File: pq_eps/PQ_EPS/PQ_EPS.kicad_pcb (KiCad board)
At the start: 4 copper layers, 40 x 40 mm, 80 parts, among them IC1 DS2782E+, IC2 ISL9120IRTNZ, J1 SLW-110-01-T-S, J2 SLW-110-01-T-S, J4 SLW-110-01-T-S, Q1 SIR424DP-T1-GE3, U1 SPV1040TTR, U2 SPV1040TTR, U3 SPV1040TTR, U4 LTC4040EUFD#PBF

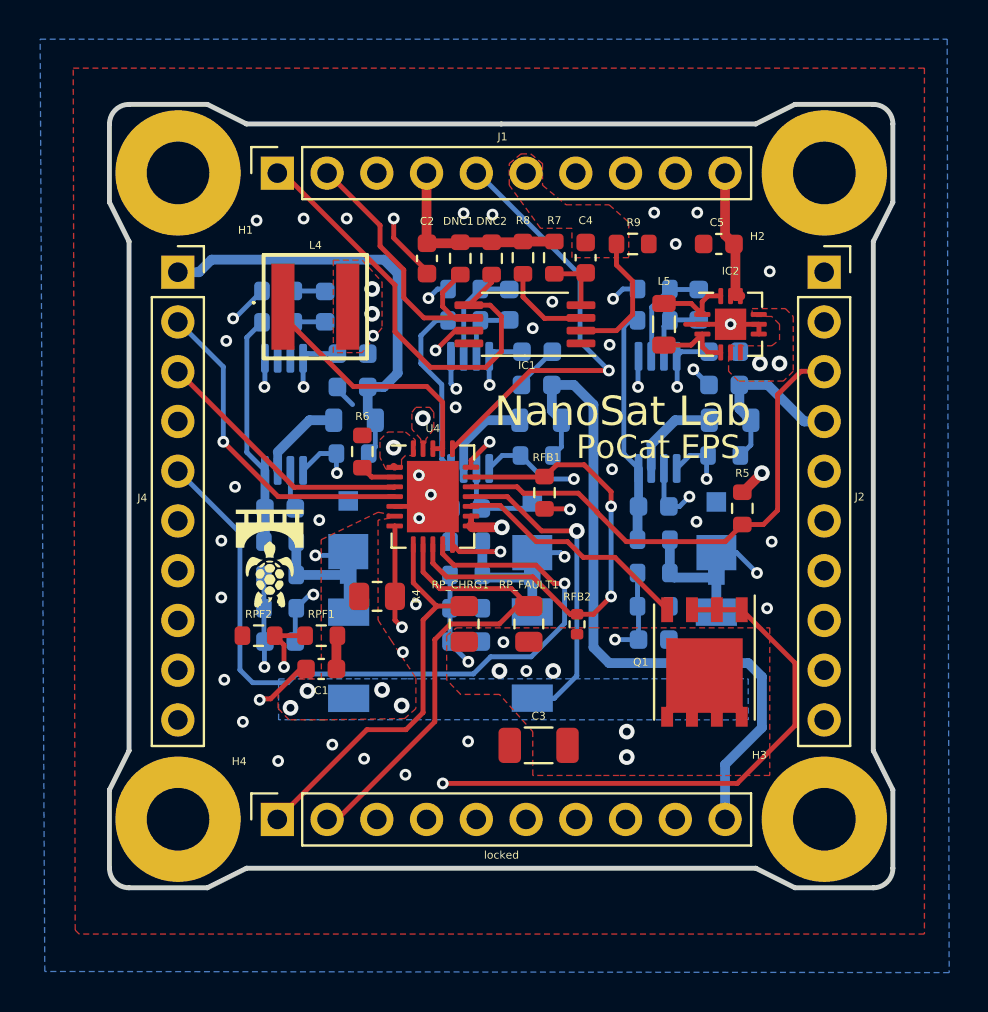
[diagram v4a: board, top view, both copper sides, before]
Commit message: Full Kicad7 transition, library improvement and adaptation, correct footprints and 3D models added
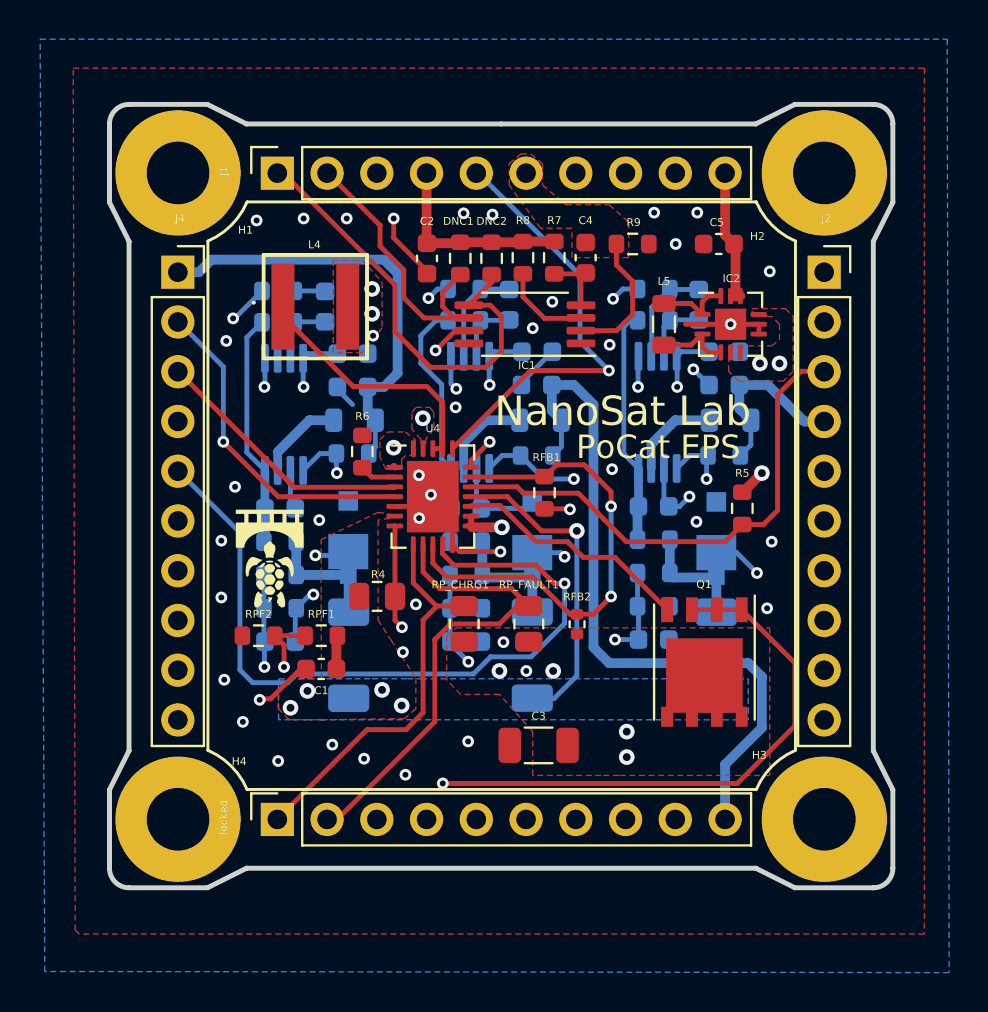
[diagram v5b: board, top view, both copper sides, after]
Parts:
- Annotation1: footprint symbols-nsl:Bridgemaker -> -nsl_symbols:Bridgemaker
- Annotation2: footprint symbols-nsl:NakNak -> -nsl_symbols:NakNak
- D1, D2, D3: footprint passive-nsl:SMM4F15ATR -> -nsl_passive:SMM4F15ATR
- D4, D5, D6: footprint Diode_SMD:D_SOD-128 -> -nsl_passive:RBS1LAM40ATR_Schottky
- IC2: footprint Package_DFN_QFN:QFN-12-1EP_3x3mm_P0.5mm_EP1.6x1.6mm -> -nsl_power:ISL9120IRTNZ
- J1, J2, J4, locked: footprint connector-nsl:SLW-110-01 -> -nsl_connector:SLW-110-01
- L4: footprint passive-nsl:XAL5030222MEC -> -nsl_passive:XAL5030222MEC
- Q1: value SIR424DP-T1-GE3 -> ~; footprint Package_SO:PowerPAK_SO-8_Single -> -nsl_power:SIR424DP

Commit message: Added adaptive resistive network for battery chemistry and charge voltage flexibility & connected all the PoLs + COMMS to 3V3_perm instead of VCC (3.3V - schottky diode)
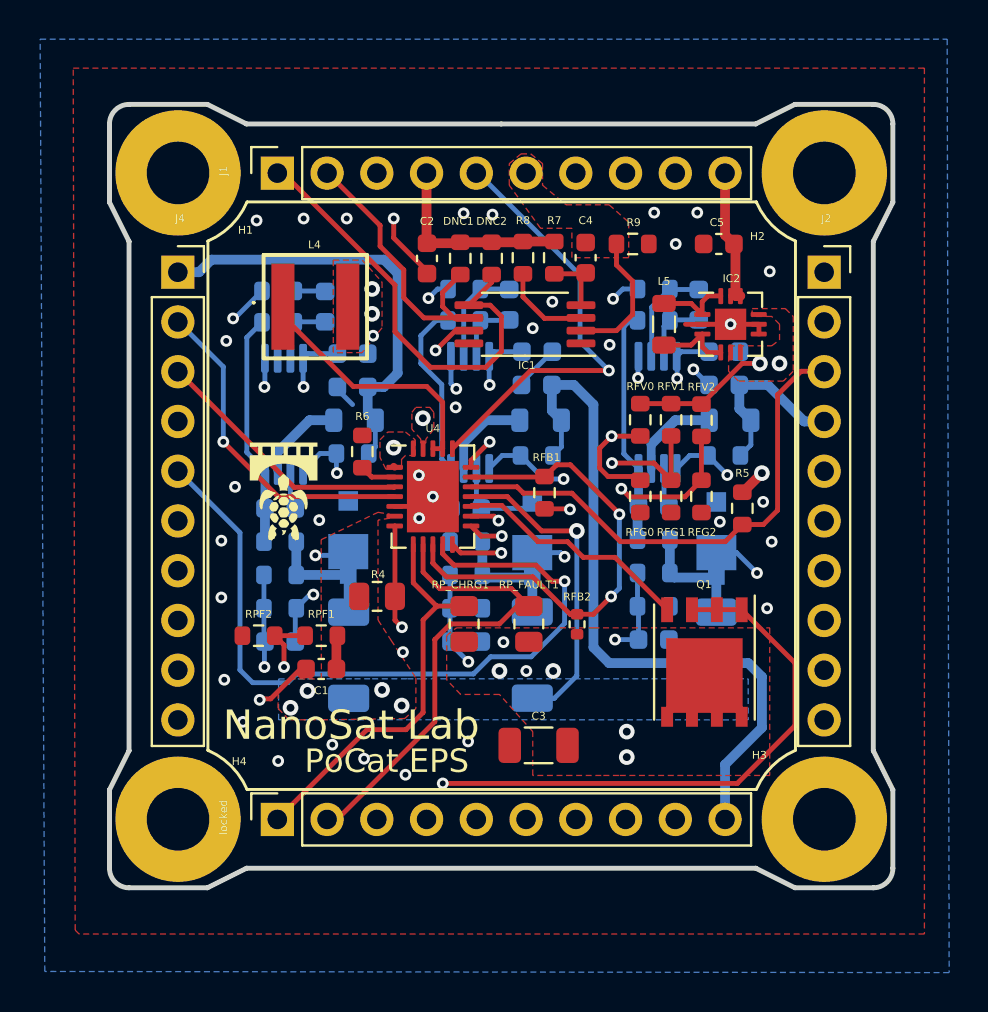
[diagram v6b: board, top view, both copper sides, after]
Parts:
- added RFG0: 1k, Resistor_SMD:R_0603_1608Metric, F.Cu at (108.8, 58.0)
- added RFG1: 1k, Resistor_SMD:R_0603_1608Metric, F.Cu at (110.4, 58.0)
- added RFG2: 1k, Resistor_SMD:R_0603_1608Metric, F.Cu at (111.9, 58.0)
- added RFV0: 1k, Resistor_SMD:R_0603_1608Metric, F.Cu at (108.8, 54.1)
- added RFV1: 1k, Resistor_SMD:R_0603_1608Metric, F.Cu at (110.4, 54.1)
- added RFV2: 1k, Resistor_SMD:R_0603_1608Metric, F.Cu at (111.9, 54.1)
- moved Annotation1 3.50 mm to (90.5, 56.3)
- moved Annotation2 3.50 mm to (90.6, 58.8)
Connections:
- U4 pad 12: GND -> /F2
- U4 pad 13: /CHOUT -> /F1
- U4 pad 14: /CHOUT -> /F0
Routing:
- net /F2: track 0.00 -> 23.7 mm, vias 0 -> 2
- net /F1: track 0.00 -> 20.0 mm, vias 0 -> 2
- net /F0: track 0.00 -> 19.8 mm, vias 0 -> 2
- net GND: track 39.3 -> 32.5 mm, vias 46 -> 43
- net /CHOUT: track 2.24 -> 7.12 mm, vias 8 -> 7
- net Net-(U2-VCTRL): track 19.6 -> 22.0 mm
- net Net-(D2-Pad1): track 28.6 -> 26.9 mm
- net Net-(U3-MPP-SET): track 15.2 -> 14.2 mm
